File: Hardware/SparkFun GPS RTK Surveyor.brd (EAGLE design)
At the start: 68.2 x 110.1 mm, 196 parts, among them J13 Internal, J16 microSD, J17 Qwiic Right Angle, J3 USB Female Type C Connector, J4 External, J5 USB Female Type C Connector, J6 Start Base, J7 Power Switch, Q2 MBT3904DW1T1, U10 MCP73833, U2 3.3V, U3 U-BLOX_ZED-F9P, U4 3.3V, U5 ESP-WROOM-32NARROW, U6 CH340C, U7 MAX17048

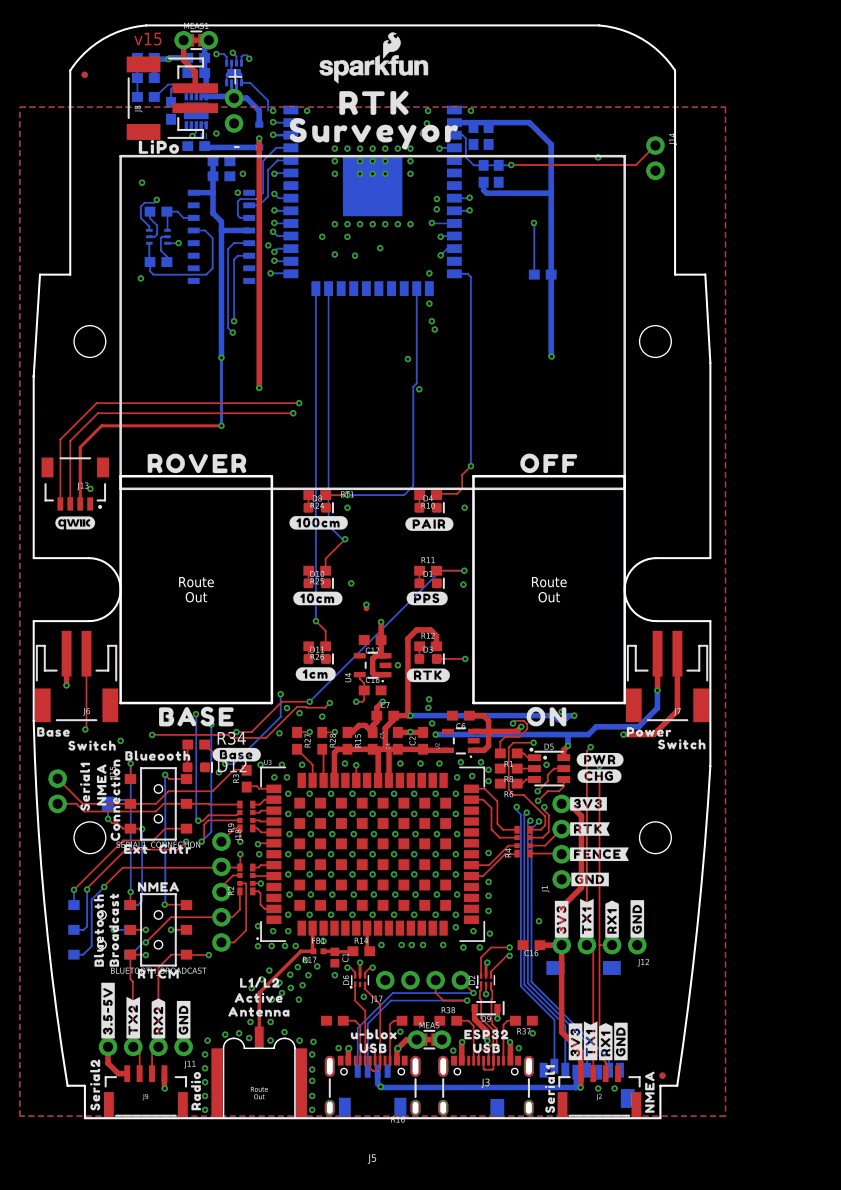
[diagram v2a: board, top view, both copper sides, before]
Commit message: Implement soft power control. Add overlay connection.
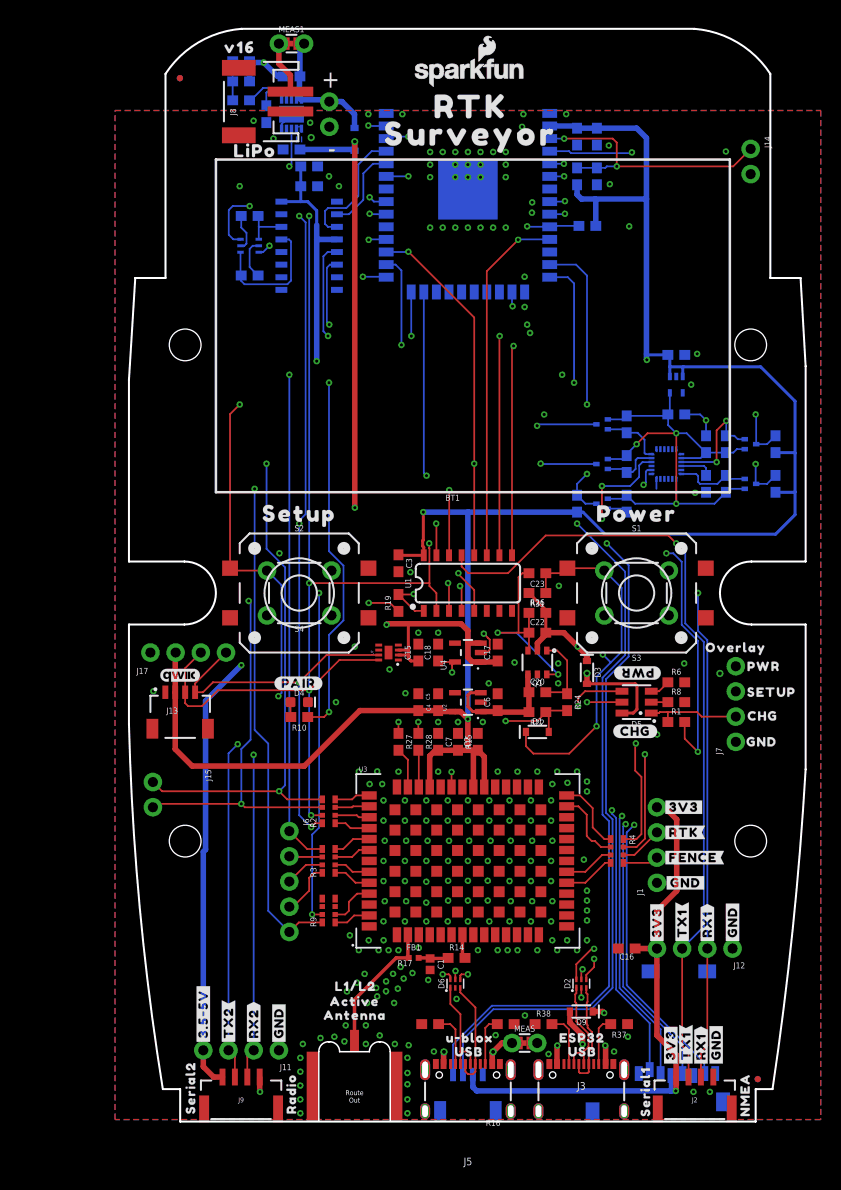
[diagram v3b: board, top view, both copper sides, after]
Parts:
- removed BLUETOOTH_BROADCAST, SERIAL1_CONNECTION, ZED_CONTROL: (no value), SparkFun-Switches:SWITCH_DPDT_SMD_AYZ0202
- removed D10, D11, D8: GREEN, SparkFun-LED:LED-0603
- removed D12: RED, SparkFun-LED:LED-0603
- removed DUAL_OUTPUT: (no value), SparkFun-Jumpers:SMT-JUMPER_2_NO_SILK
- removed J18: (no value), SparkFun-Connectors:1X05_NO_SILK
- removed R11, R25: 20, SparkFun-Resistors:0603
- removed R12, R34: 330, SparkFun-Resistors:0603
- removed U$51: (no value), output:BROADCAST3
- removed U$53: (no value), output:RTCM0
- removed U$55, U$57: (no value), output:SWITCH1
- removed U$56: (no value), output:POWER0
- removed U$58: (no value), output:BLUEOOTH3
- removed U$59: (no value), output:CNTR1
- removed U$61: (no value), output:EXT0
- removed U$62: (no value), output:NMEA2
- removed U$63: (no value), output:SERIAL10
- removed U$64: (no value), output:CONNECTION1
- removed U$69, U$75, U$77, U$78: (no value), SparkFun GPS RTK Surveyor:LIGHT_PIPE_3MM
- removed U$73: (no value), output:#DUAL#0
- removed U$79: (no value), output:#1CM#0
- removed U$80: (no value), output:#10CM#1
- removed U$81: (no value), output:#100CM#2
- removed U$89: (no value), output:DATA2
- removed U$90: (no value), output:PORT3
- removed U$91: (no value), output:PPS#RESET0
- removed U$92: (no value), output:NMEA#SERIAL1
- added C20: 10uF, SparkFun-Capacitors:0603
- added C22, C23, C3, C51, C52: 0.1uF, SparkFun-Capacitors:0603
- added C53, C54: 1.0uF, SparkFun-Capacitors:0603
- added Q1: DMC2700UDM, SparkFun-DiscreteSemi:SOT26
- added Q10, Q3, Q4, Q7, Q9: 20V/0.2A/8MHz/1.2Ω/1Vth, SparkFun-DiscreteSemi:SOT-416FL
- added R19: 1k, SparkFun-Resistors:0603
- added R22: 100k, SparkFun-Resistors:0603
- added R31: 10k, SparkFun-Resistors:0603
- added R40, R41, R44, R45, R46, R47, R48: 2.2k, SparkFun-Resistors:0603
- added R49: (no value), SparkFun-Resistors:0603
- added S1: Power, SparkFun-Switches:TACTILE_SWITCH_PTH_6.0MM
- added S2: Setup, SparkFun-Switches:TACTILE_SWITCH_PTH_6.0MM
- added S3: Power, SparkFun-Switches:TACTILE_SWITCH_SMD_12MM
- added S4: Setup, SparkFun-Switches:TACTILE_SWITCH_SMD_12MM
- added U$95: (no value), output:AG0
- added U$96: (no value), output:M0
- added U1: 74HC4052D, SparkFun-IC-Logic:SO16
- added U13: 9DoF IMU, SparkFun-Sensors:QFN24-3X3-ICM-20948
- added U14: 1.8V/100mA, SparkFun-IC-Power:SC70
- D1: value Yellow -> 250mA/100V; device SparkFun-LED:LED-0603 -> SparkFun-DiscreteSemi:SOD-323
- D3: value WHITE -> 3A/10V/280mV; device SparkFun-LED:LED-0603 -> SparkFun-DiscreteSemi:SOD-323
- J6: value Start Base -> (none); device SparkFun-Connectors:JST-2-SMD -> SparkFun-Connectors:1X05_NO_SILK
- J7: value Power Switch -> (none); device SparkFun-Connectors:JST-2-SMD -> SparkFun-Connectors:1X04_NO_SILK
- R20: value 10k -> 100k
- R24: value 20 -> 300k
- R26: value 20 -> 100k
- R3: device SparkFun-Resistors:0603 -> SparkFun-Resistors:1206_RA
- U$12: device output:#RTK#0 -> output:X1
- U$15, U$21: device SparkFun GPS RTK Surveyor:LIGHT_PIPE_3MM -> output:Y2
- U$22: device output:BASE2 -> output:X1
- U$24: device output:#PPS#1 -> output:SURVEYOR0
- U$3: device SparkFun GPS RTK Surveyor:ROCKER_SWITCH -> output:#TX_RDY#0
- U$31: device output:OFF1 -> output:POWER0
- U$33: device output:#INT#0 -> output:CHG2
- U$34: device SparkFun GPS RTK Surveyor:ROCKER_SWITCH -> output:GND3
- U$4: device output:#BASE#0 -> output:V160
- U$41: device output:BLUETOOTH2 -> output:PWR0
- U$42: device output:ON0 -> output:SETUP1
- U$44: device output:ROVER3 -> output:OVERLAY0
- U$52: device output:NMEA1 -> output:Z0
- U$54: device output:BASE0 -> output:Z0
- U$9: device output:_SURVEYOR3 -> output:SETUP0
- U2: value 3.3V -> AP2112K-3.3
- U4: value 3.3V -> ADP160
- moved U$54 75.2 mm to (50.7, 84.4), flipped to the bottom
- moved U$52 75.0 mm to (54.2, 76.2), flipped to the bottom
- moved U$41 73.8 mm to (64.8, 45.6), turned to 0 degrees
- moved U$4 71.3 mm to (12.0, 108.0)
- moved U$22 64.7 mm to (52.7, 81.2), flipped to the bottom
- moved C15 64.0 mm to (30.0, 47.0), flipped to the top, turned to 90 degrees
- moved U$44 63.5 mm to (62.0, 47.5)
- moved U7 60.4 mm to (27.0, 47.0), flipped to the top, turned to 90 degrees
- moved U$15 58.3 mm to (49.2, 76.1), flipped to the bottom
- moved U$33 56.5 mm to (64.7, 40.6), flipped to the top
- moved U$21 52.5 mm to (55.9, 84.5), flipped to the bottom
- moved J17 40.6 mm to (3.00, 47.0)
- moved C10 38.1 mm to (48.0, 99.0), turned to 270 degrees
- moved U$86 36.6 mm to (10.6, 44.5), turned to 90 degrees
- moved U$70 36.4 mm to (2.94, 44.3), turned to 90 degrees
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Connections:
- net BACKUP renamed RTC_BACKUP
- removed net 5V: C6.1, J11.4, J7.1, J9.1, U2.1, U2.3
- removed net ESP_13/LED_100CM: R24.1, U5.16
- removed net ESP_14: U5.13
- removed net ESP_15/LED_10CM: R25.1, U5.23
- removed net ESP_16/BT_RXI: BLUETOOTH_BROADCAST.2, U5.27
- removed net ESP_17/BT_TXO: BLUETOOTH_BROADCAST.5, U5.28
- removed net ESP_18/SD_SCK: J16.SCLK, U5.30
- removed net ESP_19/SD_CIPO: J16.DO/DAT0, U5.31
- removed net ESP_2/LED_1CM: R26.1, U5.24
- removed net ESP_23/SD_COPI: J16.DI/CMD, U5.37
- removed net ESP_26/ZED_TX_READY: J18.1, R9.P8, U5.11
- removed net ESP_27/ZED_!RESET!: J18.2, R2.P5, U5.12, ZED_CONTROL.4
- removed net ESP_27/ZED_!RESET!_LV: R2.P4, U3.49
- removed net ESP_36/BATT_ALRT: U5.4, U7.5
- removed net ESP_4/LED_BASE_STAT: R34.1, U5.26
- removed net ESP_5/SWITCH_BASE_SELECT: J6.1, U5.29
- removed net ESP_I34: U5.6
- removed net ESP_I39: U5.5
- removed net EXTERNAL_SERIAL1_RXI: SERIAL1_CONNECTION.4, ZED_CONTROL.6
- removed net EXTERNAL_SERIAL1_RXI/ZED_!RESET!: J12.2, J2.3, ZED_CONTROL.5
- removed net EXTERNAL_SERIAL1_TXO: DUAL_OUTPUT.2, SERIAL1_CONNECTION.1, ZED_CONTROL.3
- removed net EXTERNAL_SERIAL1_TXO/PPS: J12.3, J2.2, ZED_CONTROL.2
- removed net N$1: D3.A, R12.1
- removed net N$17: D5.CB, R1.1
- removed net N$2: D1.A, R11.1
- removed net N$26: D8.A, R24.2
- removed net N$27: D10.A, R25.2
- removed net N$29: D11.A, R26.2
- removed net NMEA-RX: BLUETOOTH_BROADCAST.6, SERIAL1_CONNECTION.6
- removed net NMEA-TX: BLUETOOTH_BROADCAST.3, DUAL_OUTPUT.1, SERIAL1_CONNECTION.3
- removed net VIN: C9.1, D2.5, D5.AB, D6.5, D7.C, D9.C, J7.2, MEAS.2, MEAS.4, U10.1, U10.2
- removed net ZED-RXI1: J15.2, R9.P5, SERIAL1_CONNECTION.5
- removed net ZED-TXO1: J15.1, R3.2, SERIAL1_CONNECTION.2
- new net CHG_LED_RES: D5.CB, J7.2, R1.1
- new net ESP_13/POWER_CTRL: D1.A, R22.1, R24.2, U5.16
- new net ESP_14/SETUP_BUTTON: J7.3, S2.1, S4.1, U5.13
- new net ESP_15/ICM_!CS!: Q9.3, R47.1, U5.23
- new net ESP_18/SCK: J16.SCLK, Q3.3, U5.30
- new net ESP_19/CIPO: J16.DO/DAT0, Q10.3, R49.1, U5.31
- new net ESP_2/MUX_A: U1.10, U5.24
- new net ESP_23/COPI: J16.DI/CMD, Q4.3, U5.37
- new net ESP_26/DAC2: U1.11, U5.11
- new net ESP_27: U5.12
- new net ESP_4/MUX_B: U1.9, U5.26
- new net ESP_5: U5.29
- new net ESP_I16/ZED-TXO1: J15.1, R2.P5, U1.12, U5.27
- new net ESP_I34/ZED_TX_READY: J6.1, R3.P5, U5.6
- new net ESP_I36/ICM_INT: Q7.3, R45.1, U5.4
- new net ESP_I39/ADC39: U1.4, U5.5
- new net ESP_O17/ZED-RXI1: J15.2, R19.2, R2.P6, U1.1
- new net EXTERNAL_DATA_IN: J12.2, J2.3, U1.3
- new net EXTERNAL_DATA_OUT: J12.3, J2.2, U1.13
- new net EXTINT_LV: R9.P2, U3.51
- new net ICM-20948-LV_!CS!: Q9.2, R46.1, U13.22
- new net ICM-20948-LV_#_1.8V: C52.1, C53.1, Q10.1, Q3.1, Q4.1, Q7.1, Q9.1, R40.2, R41.2, R44.2, R46.2, R48.2, U13.13, U13.8, U14.5
- new net ICM-20948-LV_INT: Q7.2, R44.1, U13.12
- new net ICM-20948-LV_SCK: Q3.2, R40.1, U13.23
- new net ICM-20948-LV_SDI: Q4.2, R41.1, U13.24
- new net ICM-20948-LV_SDO: Q10.2, R48.1, U13.9
- new net N$15: C22.1, C23.2, Q1.D1, Q1.G2, R26.1
- new net N$6: R19.1, U5.28
- new net N$8: C20.2, Q1.G1, R24.1
- new net POWER_BTN: C23.1, D1.C, J7.4, R31.1, S1.1, S3.1
- new net VOUT: C20.1, C6.1, Q1.D2, R22.2, U2.1, U2.3
- new net V_RAW: C22.2, C9.1, D3.C, D7.C, J11.4, J9.1, Q1.S2, R26.2, R31.2, U10.1, U10.2
- new net V_USB: D2.5, D3.A, D5.AB, D6.5, D9.C, MEAS.2, MEAS.4
- new net ZED_!RESET!: J6.3, R3.P7
- new net ZED_!RESET!_LV: R3.P2, U3.49
- new net ZED_EXTINT: R9.P7, U1.5
- net 3.3V: now also C3.1, C54.1, R45.2, R47.2, R49.2, U1.16, U14.1, U14.3; no longer R12.2
- net ESP_21/SDA: now also R2.P7, U1.2; no longer R9.P6
- net ESP_22/SCL: now also R2.P8, U1.15; no longer R9.P7
- net ESP_26/ZED_TX_READY_LV: now also R3.P4; no longer R9.P1
- net FENCE_LV: now also R4.P4; no longer R4.P8
- net GND: now also C3.2, C51.2, C52.2, C53.2, C54.2, J7.1, Q1.S1, S1.3, S2.3, S3.3, S4.3, U1.6, U1.7, U1.8, U13.18, U13.20, U14.2; no longer D1.C, D10.C, D11.C, D12.C, D8.C, J6.2
- net N$30: now also C51.1, U13.10; no longer D12.A, R34.2
- net PPS: now also R9.P1; no longer R2.P1
- net RTK_LV: now also R4.P3; no longer R4.P7
- net RX2_LV: now also R4.P2; no longer R4.P6
- net RXLV: now also R2.P3; no longer R9.P4
- net SCL_LV: now also R2.P1; no longer R9.P2
- net SDA_LV: now also R2.P2; no longer R9.P3
- net TX2_LV: now also R4.P1; no longer R4.P5
- net TXLV: now also R2.P4; no longer R3.1
- net ZED-RXI2: now also R4.P7; no longer BLUETOOTH_BROADCAST.4, R4.P3
- net ZED-TXO2: now also R4.P8; no longer BLUETOOTH_BROADCAST.1, R4.P4
- net ZED_!SAFE!: now also J6.4, R3.P8; no longer J18.3, R2.P6
- net ZED_!SAFE!_LV: now also R3.P1; no longer R2.P3
- net ZED_D_SEL: now also J6.2, R3.P6; no longer J18.5, R2.P7
- net ZED_D_SEL_LV: now also R3.P3; no longer R2.P2
- net ZED_FENCE_STAT: now also R4.P5; no longer R4.P1
- net ZED_PPS_STAT: now also J6.5, R9.P8, U1.14; no longer J18.4, R11.2, R2.P8, ZED_CONTROL.1
- net ZED_RTK_STAT: now also R4.P6; no longer D3.C, R4.P2
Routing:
- net VIN: track 189.6 -> 0.00 mm, vias 9 -> 0
- net V_RAW: track 0.00 -> 149.4 mm, vias 0 -> 5
- net ESP_19/CIPO: track 0.00 -> 143.0 mm, vias 0 -> 5
- net ESP_14/SETUP_BUTTON: track 0.00 -> 133.0 mm, vias 0 -> 3
- net ESP_23/COPI: track 0.00 -> 127.2 mm, vias 0 -> 4
- net ESP_23/SD_COPI: track 120.9 -> 0.00 mm, vias 3 -> 0
- net ESP_18/SCK: track 0.00 -> 120.2 mm, vias 0 -> 4
- net ESP_19/SD_CIPO: track 115.8 -> 0.00 mm, vias 3 -> 0
- net ESP_18/SD_SCK: track 113.2 -> 0.00 mm, vias 3 -> 0
- net 5V: track 112.3 -> 0.00 mm, vias 2 -> 0
- net ESP_I16/ZED-TXO1: track 0.00 -> 108.4 mm, vias 0 -> 4
- net ESP_27/ZED_!RESET!: track 102.6 -> 0.00 mm, vias 4 -> 0
- net EXTERNAL_SERIAL1_TXO/PPS: track 101.6 -> 0.00 mm, vias 2 -> 0
- net ESP_I34/ZED_TX_READY: track 0.00 -> 100.1 mm, vias 0 -> 3
- net EXTERNAL_SERIAL1_RXI/ZED_!RESET!: track 99.7 -> 0.00 mm, vias 3 -> 0
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- added copper zone on layer 16, net V_RAW
- removed copper zone on layer 16, net VIN
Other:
- outline, holes or cut-outs redrawn
- board text added: "11.9+2.75=14.65mm"
- board text added: "11.9-3.4=8.5mm actuator length on square button"
- board text added: "11.9-8=3.9"
- board text added: "18.5-5-1.6=11.9mm"
- board text added: "Distance from PCB surface to outer surface of lid:"
- board text added: "Distance from inner lid to PCB surface:"
- board text removed: "-ND"
- board text removed: "10.16mm / 0.4" is common"
- board text removed: "12.7mm / 0.5" is common"
- board text removed: "12x12mm switch height: 8.5mm"
- board text removed: "350-3725-ND (Flat $0.25)"
- board text removed: "350-3726-ND (Flat $0.25)"
- board text removed: "350-3738-ND (Dome $0.25)"
- board text removed: "Gap to base switch: 3.4mm"
- board text removed: "Inside height: 18.5mm"
- board text removed: "LED Height: 0.8mm"
- board text removed: "NA"
- board text removed: "Pipe length: 12.08-12.85mm"
- board text removed: "Recommended air gap: 0.5-1.27mm"
- board text removed: "Rocker height: 16.7mm"
- board text removed: "Route Out"
- board text removed: "Thckness of top cover: 2.25mm"
- board text removed: "Top Cover thickness: 2.25mm"
- board text removed: "Top PCB surface to inside lid: 11.9mm"
- board text removed: "v15"

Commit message: Update soft power switch MOSFET
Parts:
- Q1: value DMC2700UDM -> SIL2308-TP
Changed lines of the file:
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@@
 <setting verticaltext="up"/>
 </settings>
-<grid distance="1" unitdist="mm" unit="mm" style="lines" multiple="1" display="yes" altdistance="0.1" altunitdist="mm" altunit="mm"/>
+<grid distance="0.05" unitdist="inch" unit="inch" style="lines" multiple="1" display="yes" altdistance="0.005" altunitdist="inch" altunit="inch"/>
 <layers>
 <layer number="1" name="Top/Horz" color="4" fill="1" visible="yes" active="yes"/>
-<layer number="2" name="GND/Horz" color="1" fill="3" visible="yes" active="yes"/>
-<layer number="15" name="Vert" color="4" fill="6" visible="yes" active="yes"/>
+<layer number="2" name="GND/Horz" color="1" fill="3" visible="no" active="yes"/>
+<layer number="15" name="Vert" color="4" fill="6" visible="no" active="yes"/>
 <layer number="16" name="Bottom/Vert" color="1" fill="1" visible="yes" active="yes"/>
 <layer number="17" name="Pads" color="2" fill="1" visible="yes" active="yes"/>
@@
 <layer number="47" name="Measures" color="7" fill="1" visible="no" active="yes"/>
 <layer number="48" name="Document" color="7" fill="1" visible="no" active="yes"/>
-<layer number="49" name="Reference" color="7" fill="1" visible="yes" active="yes"/>
+<layer number="49" name="Reference" color="7" fill="1" visible="no" active="yes"/>
 <layer number="50" name="dxf" color="7" fill="1" visible="no" active="yes"/>
 <layer number="51" name="tDocu" color="6" fill="1" visible="yes" active="yes"/>
@@
 </element>
 <element name="U$3" library="output" package="#TX_RDY#0" value="" x="12.6" y="29" smashed="yes" rot="MR0"/>
-<element name="Q1" library="SparkFun-DiscreteSemi" package="SOT26" value="DMC2700UDM" x="42" y="46" smashed="yes" rot="R180">
+<element name="Q1" library="SparkFun-DiscreteSemi" package="SOT26" value="SIL2308-TP" x="42" y="46" smashed="yes" rot="R180">
 <attribute name="NAME" x="42" y="44.222" size="0.6096" layer="25" font="vector" ratio="20" rot="R180" align="bottom-center"/>
-<attribute name="PROD_ID" value="TRANS-11993" x="48.35" y="39.65" size="1.778" layer="27" font="vector" ratio="15" rot="R180" display="off"/>
+<attribute name="PROD_ID" value="TRANS-15717" x="48.35" y="39.65" size="1.778" layer="27" font="vector" ratio="15" rot="R180" display="off"/>
 <attribute name="VALUE" x="42" y="47.778" size="0.6096" layer="27" font="vector" ratio="20" rot="R180" align="top-center"/>
 </element>
